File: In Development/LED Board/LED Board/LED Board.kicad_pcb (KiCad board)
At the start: 2 copper layers, 30 x 30 mm, 9 parts, among them J1 Screw_Terminal_01x03, U1 AL5802

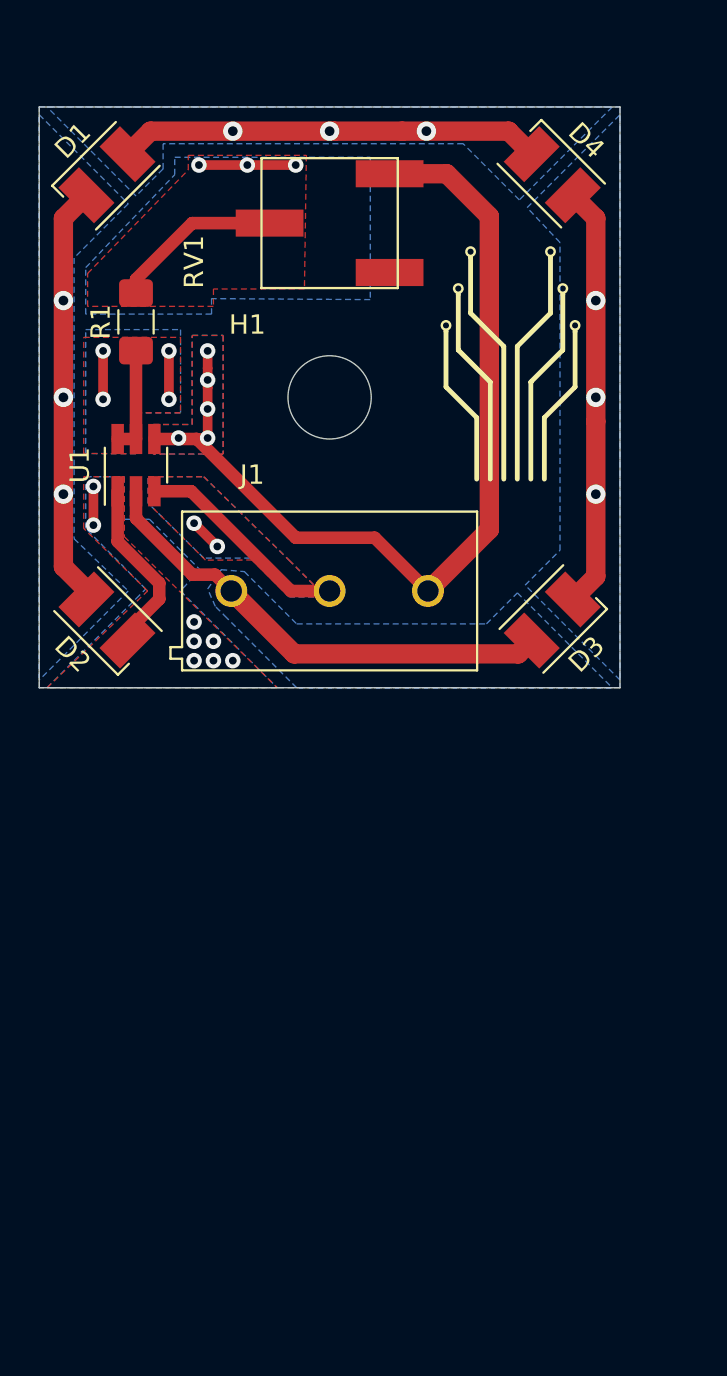
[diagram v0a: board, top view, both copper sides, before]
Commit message: MFRC522 silkscreen edit, LED thermal improvement
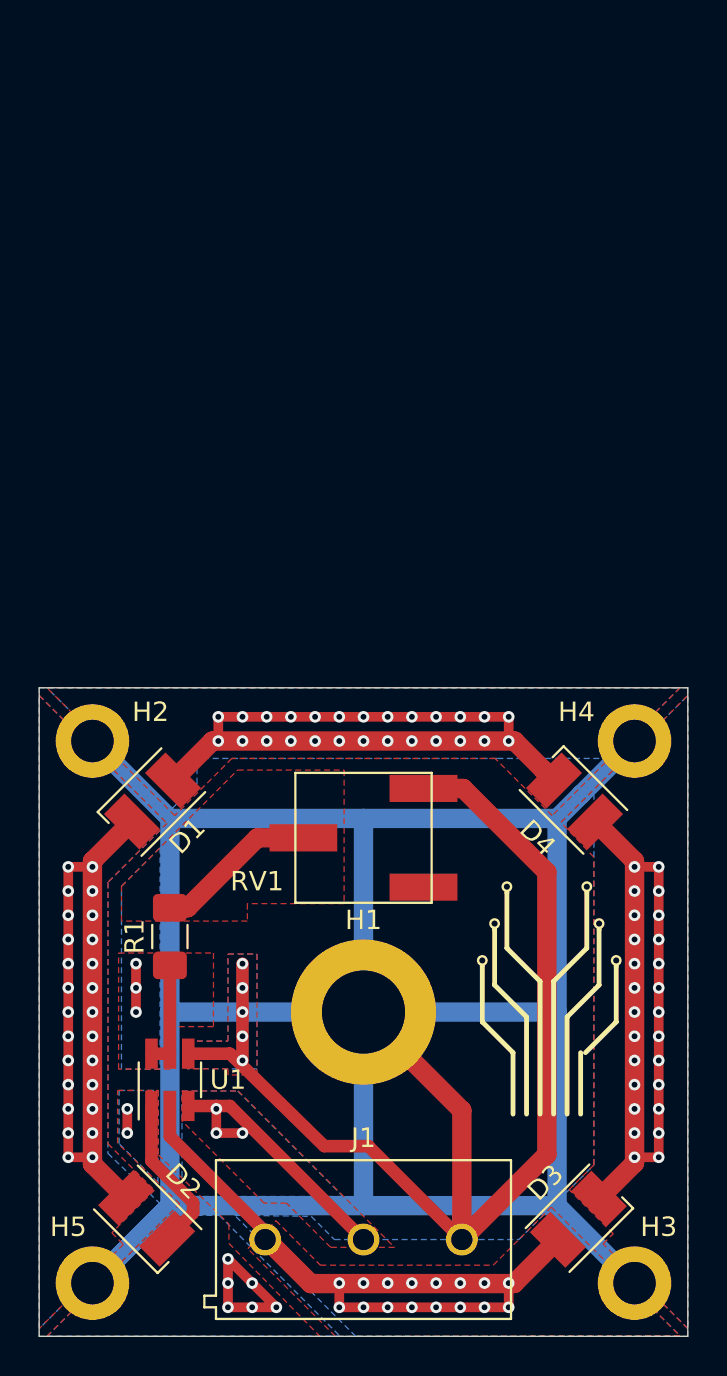
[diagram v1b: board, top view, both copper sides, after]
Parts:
- added H2: MountingHole, MountingHole:MountingHole_2.2mm_M2_DIN965_Pad, F.Cu at (102.8, 102.8)
- added H3: MountingHole, MountingHole:MountingHole_2.2mm_M2_DIN965_Pad, F.Cu at (130.8, 130.8)
- added H4: MountingHole, MountingHole:MountingHole_2.2mm_M2_DIN965_Pad, F.Cu at (130.8, 102.8)
- added H5: MountingHole, MountingHole:MountingHole_2.2mm_M2_DIN965_Pad, F.Cu at (102.8, 130.8)
- H1: footprint MountingHole:MountingHole_4.3mm_M4 -> MountingHole:MountingHole_4.3mm_M4_DIN965_Pad
- moved J1 33.5 mm to (116.8, 128.5)
- moved D1 32.4 mm to (105.8, 105.8)
- moved D4 32.4 mm to (127.7, 105.8)
- moved H1 31.8 mm to (116.8, 116.8)
- moved R1 31.8 mm to (106.8, 112.8)
- moved RV1 31.8 mm to (116.8, 107.8)
- moved U1 31.8 mm to (106.8, 120.2)
- moved D3 31.0 mm to (127.8, 127.5)
- moved D2 31.0 mm to (105.5, 127.4)
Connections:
- H1 pad 1: (no net) -> GND
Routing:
- net GND: track 50.1 -> 216.0 mm
- net Net-(D1-Pad1): track 21.4 -> 38.5 mm, vias 3 -> 26
- net Net-(D1-Pad2): track 21.9 -> 38.9 mm, vias 3 -> 26
- net Net-(D3-Pad1): track 21.9 -> 38.6 mm, vias 3 -> 26
- net VCC: track 25.0 -> 37.3 mm, vias 0 -> 16
- net Net-(D2-Pad1): track 10.8 -> 18.1 mm
- net Net-(R1-Pad2): track 13.8 -> 8.40 mm, vias 3 -> 0
- net Net-(R1-Pad1): track 10.5 -> 8.01 mm, vias 4 -> 3
- net /EN: track 12.9 -> 14.7 mm, vias 2 -> 3
- added copper zone on F.Cu, net Net-(D1-Pad1)
- added copper zone on F.Cu, net Net-(D1-Pad2)
- added copper zone on F.Cu, net Net-(D3-Pad1)
- added copper zone on F.Cu, net VCC
- removed copper zone on B.Cu, net Net-(R1-Pad2)
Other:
- board size 30 x 30 mm -> 33.5 x 33.5 mm

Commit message: In production.
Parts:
- added FID1: Fiducial, Fiducial:Fiducial_0.5mm_Mask1mm, F.Cu at (106.5, 98.2)
- added FID2: Fiducial, Fiducial:Fiducial_0.5mm_Mask1mm, F.Cu at (127.0, 98.2)
- added FID3: Fiducial, Fiducial:Fiducial_0.5mm_Mask1mm, F.Cu at (116.8, 68.6)
- added TP1: TestPoint, TestPoint:TestPoint_Pad_1.0x1.0mm, B.Cu at (128.5, 95.0)
- added TP2: TestPoint, TestPoint:TestPoint_Pad_1.0x1.0mm, B.Cu at (105.0, 71.5)
- added TP3: TestPoint, TestPoint:TestPoint_Pad_1.0x1.0mm, B.Cu at (105.0, 95.0)
- added TP4: TestPoint, TestPoint:TestPoint_Pad_1.0x1.0mm, B.Cu at (128.5, 71.5)
- H1: footprint MountingHole:MountingHole_4.3mm_M4_DIN965_Pad -> Custom:Hole_10mm
- moved D1 33.5 mm to (105.8, 72.3)
- moved D2 33.5 mm to (105.5, 93.9)
- moved D3 33.5 mm to (127.8, 94.0)
- moved D4 33.5 mm to (127.7, 72.3)
- moved H1 33.5 mm to (116.8, 83.2)
- moved H2 33.5 mm to (102.8, 69.2)
- moved H3 33.5 mm to (130.8, 97.2)
- moved H4 33.5 mm to (130.8, 69.2)
- moved H5 33.5 mm to (102.8, 97.2)
- moved J1 33.5 mm to (116.8, 95.0)
- moved R1 33.5 mm to (106.8, 79.3)
- moved RV1 33.5 mm to (116.8, 74.2)
- moved U1 33.5 mm to (106.8, 86.8)
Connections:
- H2 pad 1: GND -> (no net)
- H3 pad 1: GND -> (no net)
- H4 pad 1: GND -> (no net)
- H5 pad 1: GND -> (no net)
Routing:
- net GND: track 216.0 -> 143.8 mm
- net Net-(D1-Pad2): track 38.9 -> 50.5 mm, vias 26 -> 24
